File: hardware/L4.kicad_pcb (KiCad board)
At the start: 2 copper layers, 374.6 x 99.7 mm, 136 parts, among them J1 JST_PH, J2 JST_PH, Q1 SSM3J332R, Q2 SSM3J332R, SW1 SW_Push, SW10 SW_Push, SW11 SW_Push, SW12 SW_Push, SW13 SW_Push, SW14 SW_Push, SW15 SW_Push, SW16 SW_Push, SW17 SW_Push, SW18 SW_Push, SW19 SW_Push, SW2 SW_Push, SW20 SW_Push, SW21 SW_Push, SW22 SW_Push, SW23 SW_Push, SW24 SW_Push, SW25 SW_Push, SW26 SW_Push, SW27 SW_DP3T, SW28 SW_Push, SW29 SW_Push, SW3 SW_Push, SW30 SW_Push, SW31 SW_Push, SW32 SW_Push, SW33 SW_Push, SW34 SW_Push, SW35 SW_Push, SW36 SW_Push, SW37 SW_Push, SW38 SW_Push, SW39 SW_Push, SW4 SW_Push, SW40 SW_Push, SW41 SW_Push, SW42 SW_Push, SW43 SW_Push, SW44 SW_Push, SW45 SW_Push, SW46 SW_Push, SW47 SW_Push, SW48 SW_Push, SW49 SW_Push, SW5 SW_Push, SW50 SW_Push, SW51 SW_Push, SW52 SW_Push, SW53 SW_Push, SW54 SW_DP3T, SW6 SW_Push, SW7 SW_Push, SW8 SW_Push, SW9 SW_Push, U1 XIAO nRF52840, U2 XIAO nRF52840

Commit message: finish routing
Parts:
- C1, C2: value 4.7u -> 100u; footprint Capacitor_SMD:C_0805_2012Metric_Pad1.18x1.45mm_HandSolder -> Capacitor_SMD:C_1206_3216Metric_Pad1.33x1.80mm_HandSolder
- moved C2 46.1 mm to (224.0, 155.1), turned to 180 degrees
- moved Q2 46.1 mm to (224.0, 129.1)
- moved J2 42.6 mm to (255.9, 141.9)
- moved D29 38.3 mm to (255.5, 120.5)
- moved D35 38.2 mm to (255.5, 136.5)
- moved D30 38.1 mm to (274.5, 120.5)
- moved D31 38.1 mm to (293.6, 120.5)
- moved D32 38.1 mm to (312.6, 120.5)
- moved D36 38.1 mm to (274.5, 139.5)
- moved D37 38.1 mm to (293.6, 139.5)
- moved D38 38.1 mm to (312.6, 139.5)
- moved D42 38.1 mm to (274.5, 158.6)
- moved D43 38.1 mm to (293.6, 158.6)
- moved D44 38.1 mm to (312.6, 158.6)
- moved D48 38.1 mm to (274.5, 177.6)
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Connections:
- U1 pad 10: COL4_L -> COL3_L
- U1 pad 11: COL5_L -> COL2_L
- U1 pad 8: COL2_L -> COL5_L
- U1 pad 9: COL3_L -> COL4_L
- U2 pad 1: ROW0_R -> ROW1_R
- U2 pad 10: COL4_R -> COL5_R
- U2 pad 11: COL5_R -> ROW0_R
- U2 pad 2: ROW1_R -> ROW2_R
- U2 pad 3: ROW2_R -> ROW3_R
- U2 pad 4: ROW3_R -> ROW4_R
- U2 pad 5: ROW4_R -> COL2_R
- U2 pad 6: COL0_R -> COL1_R
- U2 pad 7: COL1_R -> COL0_R
- U2 pad 8: COL2_R -> COL3_R
- U2 pad 9: COL3_R -> COL4_R
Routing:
- net COL0_L: track 0.00 -> 192.8 mm, vias 0 -> 1
- net ROW3_R: track 0.00 -> 191.9 mm, vias 0 -> 1
- net COL5_R: track 0.00 -> 186.3 mm
- net ROW2_R: track 0.00 -> 179.0 mm, vias 0 -> 1
- net COL3_L: track 0.00 -> 177.1 mm, vias 0 -> 1
- net COL1_L: track 0.00 -> 172.7 mm, vias 0 -> 1
- net COL2_L: track 0.00 -> 172.6 mm, vias 0 -> 1
- net COL2_R: track 0.00 -> 168.9 mm, vias 0 -> 1
- net COL4_R: track 0.00 -> 166.2 mm
- net ROW3_L: track 0.00 -> 162.8 mm
- net ROW1_R: track 0.00 -> 161.0 mm, vias 0 -> 1
- net COL4_L: track 0.00 -> 157.0 mm, vias 0 -> 1
- net ROW2_L: track 0.00 -> 149.6 mm
- net COL1_R: track 0.00 -> 148.8 mm, vias 0 -> 1
- net COL3_R: track 0.00 -> 146.1 mm
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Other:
- board size 374.6 x 99.7 mm -> 336.5 x 99.7 mm
- board text added: "C"
- board text added: "L"

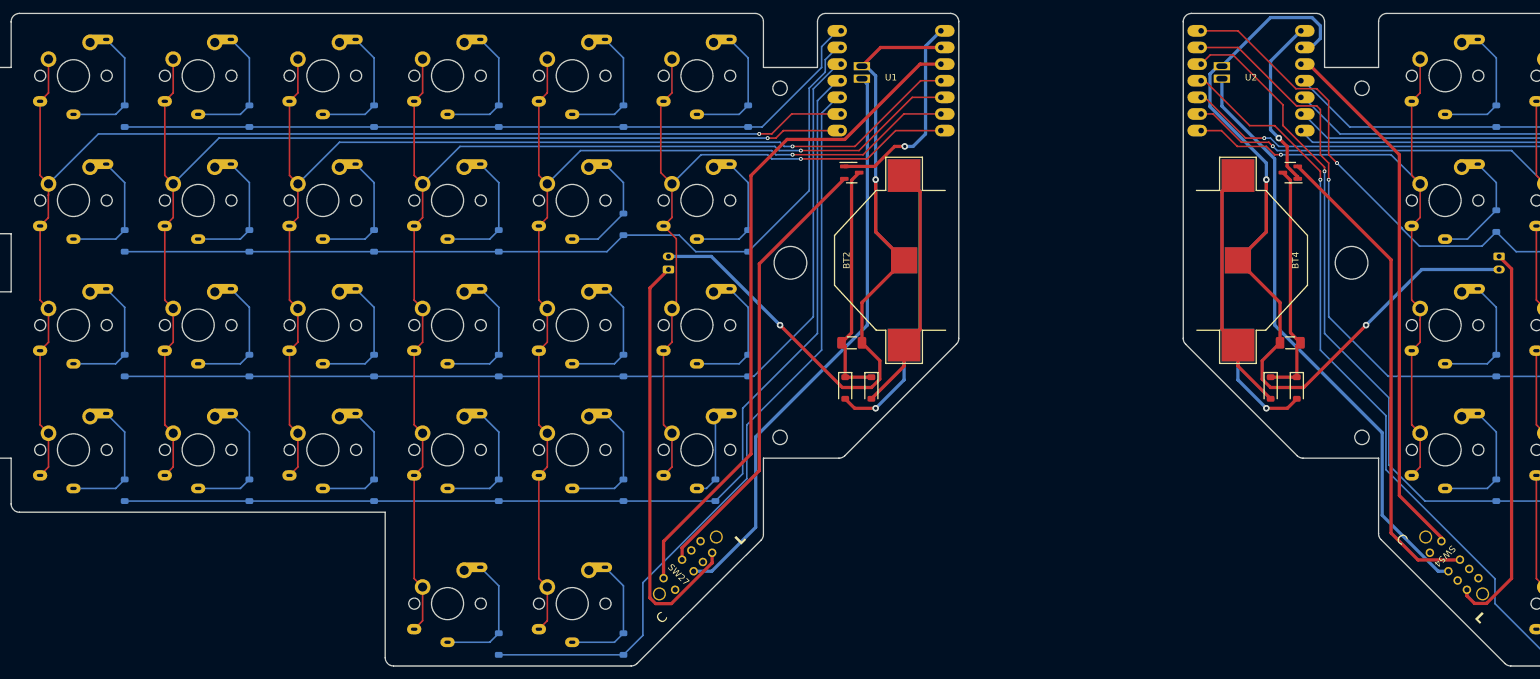
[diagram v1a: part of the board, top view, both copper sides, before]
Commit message: fillet left half
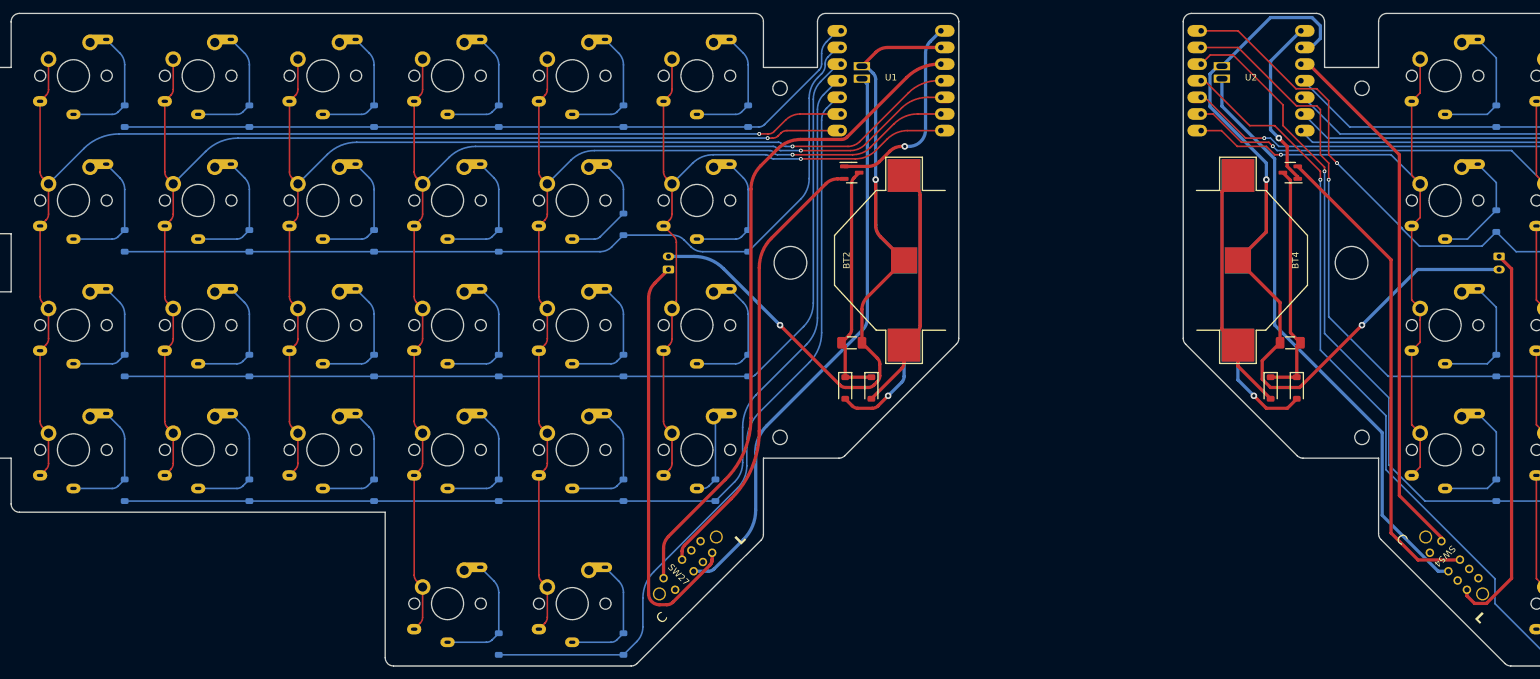
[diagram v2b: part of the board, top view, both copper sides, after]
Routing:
- net VCC_L: track 103.1 -> 101.5 mm
- net COL5_L: track 113.2 -> 111.7 mm
- net ROW4_L: track 118.3 -> 116.9 mm
- net COL3_L: track 177.1 -> 175.8 mm
- net COL4_L: track 157.0 -> 155.7 mm
- net COL2_L: track 172.6 -> 171.4 mm
- net GND_L: track 123.1 -> 122.0 mm
- net COL0_L: track 192.8 -> 191.8 mm
- net ROW3_L: track 162.8 -> 161.8 mm
- net ROW1_L: track 134.8 -> 133.8 mm
- net COL1_L: track 172.7 -> 171.9 mm
- net VBATT_L: track 88.2 -> 87.5 mm

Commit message: apply fillets
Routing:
- net Net-(BT3-+): track 44.6 -> 16.5 mm
- net Net-(BT4-+): track 38.2 -> 10.2 mm
- net Net-(BT2-+): track 38.0 -> 10.2 mm
- net Net-(BT1-+): track 44.3 -> 16.5 mm
- net GND_R: track 140.5 -> 142.6 mm
- net ROW4_R: track 142.6 -> 140.9 mm
- net ROW3_R: track 191.9 -> 190.5 mm
- net VBUS_R: track 26.3 -> 27.6 mm
- net ROW2_R: track 179.0 -> 177.8 mm
- net VBATT_R: track 90.5 -> 89.4 mm
- net COL1_R: track 148.8 -> 147.8 mm
- net COL0_R: track 104.2 -> 103.2 mm
- net COL2_R: track 168.9 -> 167.9 mm
- net VCC_R: track 82.5 -> 81.5 mm
- net COL4_R: track 166.2 -> 165.3 mm
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- added copper zone on B.Cu, net GND_L
- added copper zone on F.Cu, net GND_L
- added copper zone on B.Cu, net GND_R
- added copper zone on F.Cu, net GND_R
